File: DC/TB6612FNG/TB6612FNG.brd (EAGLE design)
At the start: 25.4 x 25.4 mm, 13 parts

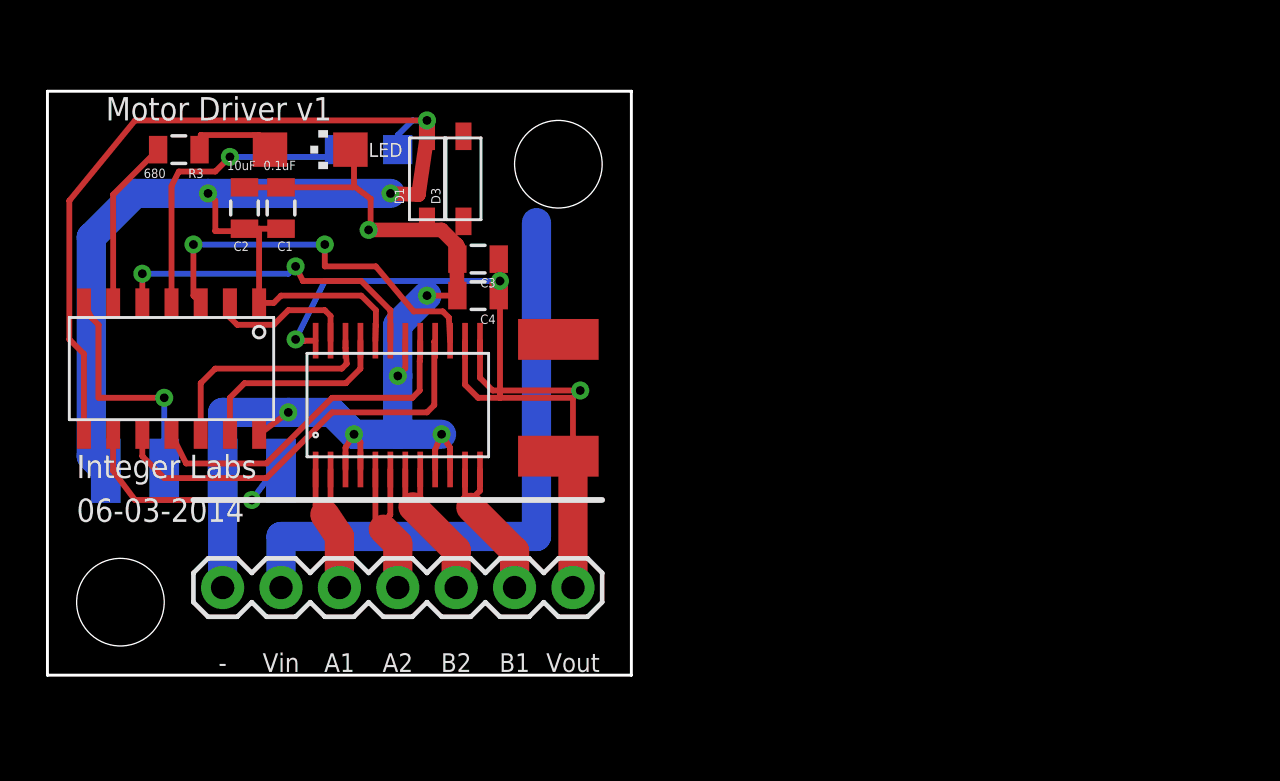
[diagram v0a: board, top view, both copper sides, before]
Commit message: Mostly re-routed the TB6612FNG based motor driver board for the v2 footprint. Not finished, since I'm planning to abandon this chip.
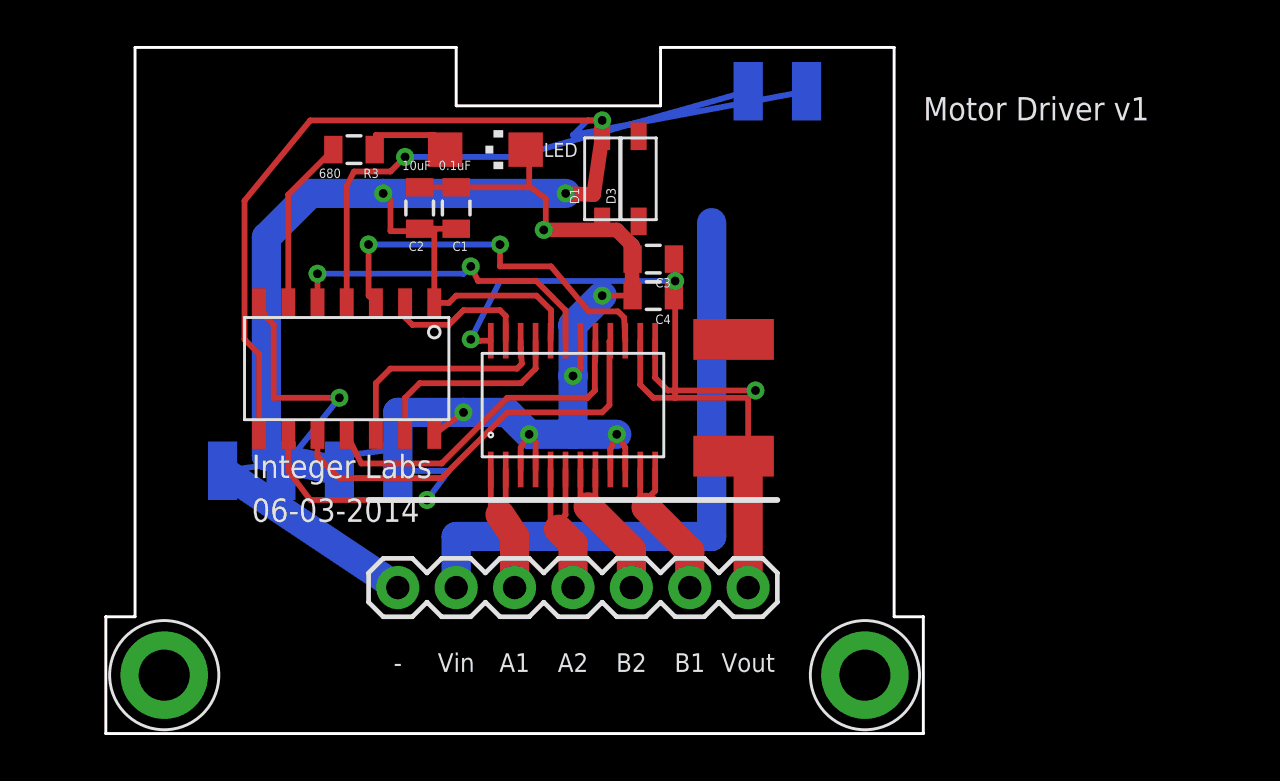
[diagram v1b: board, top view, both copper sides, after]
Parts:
- U$4: value FOOTPRINT -> FOOTPRINTFOOTPRINT-2; device IntegerLabs:FOOTPRINT -> IntegerLabs:FOOTPRINT2
- moved C1 7.62 mm to (17.8, 20.3)
- moved D3 7.62 mm to (25.7, 21.6)
- moved JP2 7.62 mm to (30.5, 3.81)
- moved LED 7.62 mm to (19.1, 22.9)
- moved R3 7.62 mm to (13.3, 22.9)
- moved U$3 7.62 mm to (16.8, 13.0)
- moved C2 7.62 mm to (16.2, 20.3)
- moved U$1 7.62 mm to (22.9, 11.7)
- moved C3 7.62 mm to (26.4, 18.1)
- moved C4 7.62 mm to (26.4, 16.5)
- moved D1 7.62 mm to (24.1, 21.6)
- moved U$2 7.62 mm to (29.8, 12.1)
- moved U$4 3.59 mm to (2.54, -2.54)
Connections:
- net GND: now also U$4.GND; no longer U$4.P$3
- net SCL/SCK: now also U$4.SCL; no longer U$4.P$4
- net SDA/MOSI: now also U$4.SDA; no longer U$4.P$2
- net VCC: now also U$4.VCC; no longer U$4.P$1
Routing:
- net GND: track 51.0 -> 61.8 mm
- net RESET: track 13.4 -> 23.6 mm
- net MISO: track 29.8 -> 39.5 mm
- net VCC: track 42.7 -> 45.1 mm
- net SCL/SCK: track 10.2 -> 12.1 mm
- net SDA/MOSI: track 10.4 -> 11.3 mm
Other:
- board size 25.4 x 25.4 mm -> 35.6 x 29.8 mm
